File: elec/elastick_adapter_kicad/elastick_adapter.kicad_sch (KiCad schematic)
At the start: 12 parts, among them J2 DE9_Pins_MountingHoles

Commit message: update kicad
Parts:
- removed R12, R13, R14, R16, R17, R25, R26, R27, R4: 330, Resistor_THT:R_Axial_DIN0207_L6.3mm_D2.5mm_P7.62mm_Horizontal, symbol Device:R
- added C1: 470µF, Capacitor_THT:CP_Radial_D8.0mm_P3.50mm, symbol Device:C_Polarized
- added C2: 100nF, Capacitor_THT:C_Disc_D5.0mm_W2.5mm_P5.00mm, symbol Device:C
- added C3, C4: 22nF, Capacitor_THT:C_Disc_D5.0mm_W2.5mm_P5.00mm, symbol Device:C
- added J2: USB-C Breakout, elastick:usbc, symbol elastick:usbc
- added SW1: POWER, Button_Switch_THT:SW_Slide_SPDT_Angled_CK_OS102011MA1Q, symbol Switch:SW_SPDT
- added SW2: ROTARY_SWITCH, Rotary_Encoder:RotaryEncoder_Alps_EC11E-Switch_Vertical_H20mm, symbol Device:RotaryEncoder_Switch
- DS1: renamed from U2; value ~ -> SSD1306 I2C OLED
- J1: renamed from J2; value DE9_Pins_MountingHoles -> DE-9JOYSTICK
- U1: value ~ -> LOLIN-D32
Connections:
- net at J1.3: now also U1.9 (26)
- net at U1.13: now also J1.5, C4.2
- net at J1.7: now also U1.8 (25)
- net at U1.11 (14): now also J1.4
- net at U1.12: now also J1.9, C3.2
- net at DS1.1 (vcc): now also U1.1 (3v), C1.1, C2.1
- net at DS1.2 (gnd): now also U1.17 (gnd), U1.32 (gnd), C1.2, C2.2, C3.1, C4.1, SW1.1 (A), SW2.C, SW2.S1
- net at DS1.3 (scl): now also U1.22 (21)
- net at DS1.4 (sda): now also U1.21 (3)
- net at U1.10 (27): now also J1.8
- net at U1.14 (enable): now also SW1.2 (B)
- net at U1.26 (17): now also J1.2
- net at U1.27 (16): now also J1.6
- net at U1.28 (4): now also J1.1
- net at U1.5 (34): now also SW2.B
- net at U1.6 (32): now also SW2.A
- net at U1.7 (33): now also SW2.S2
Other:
- moved on the sheet: DS1, J1, U1

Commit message: update kicad
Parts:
- SW1: footprint Button_Switch_THT:SW_Slide_SPDT_Angled_CK_OS102011MA1Q -> elastick:SW_90degrees_3pins
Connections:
- net at C1.2, C2.2, C3.1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: now also SW1.2 (B), SW2.A, SW2.S2; no longer SW1.1 (A), SW2.C, SW2.S1
- net at DS1.3 (scl): now also U1.19 (22); no longer U1.22 (21)
- net at DS1.4 (sda): now also U1.22 (21); no longer U1.21 (3)
- net at U1.14 (enable): now also SW1.3 (C); no longer SW1.2 (B)
- net at U1.23 (19): now also SW2.C
- net at U1.24 (18): now also SW2.B
- net at U1.25 (5): now also SW2.S1
- net at U1.5 (34): no longer SW2.B
- net at U1.6 (32): no longer SW2.A
- net at U1.7 (33): no longer SW2.S2
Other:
- moved on the sheet: SW2

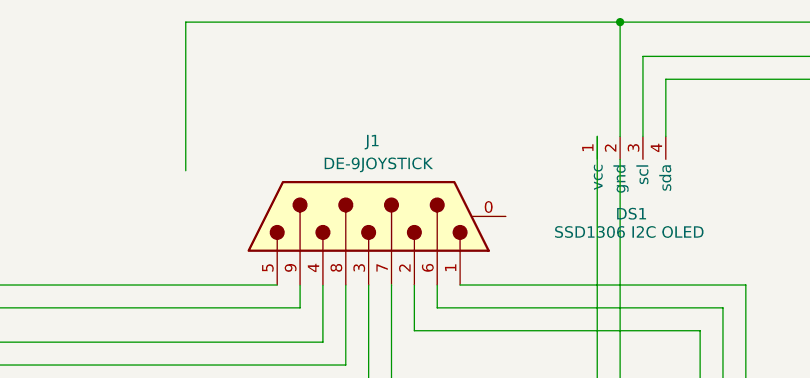
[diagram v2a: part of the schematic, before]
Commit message: update kicad with 3d for rotary button
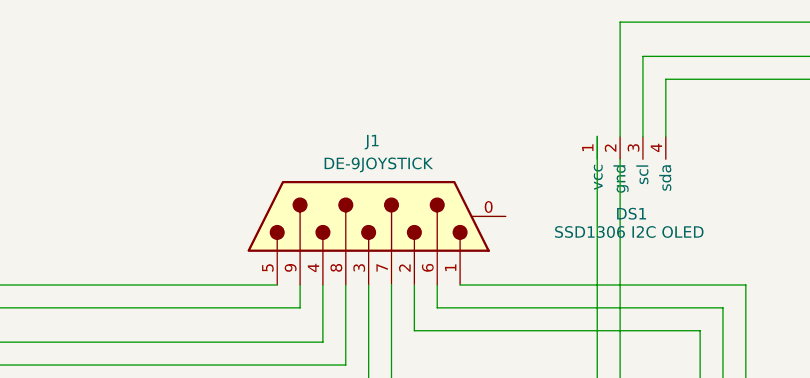
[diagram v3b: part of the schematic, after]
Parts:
- SW2: footprint Rotary_Encoder:RotaryEncoder_Alps_EC11E-Switch_Vertical_H20mm -> elastick:rotary_encoder
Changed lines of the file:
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@@
-	)
-	(junction
-		(at 179.07 16.51)
-		(diameter 0)
-		(color 0 0 0 0)
 	)
 	(junction
@@
 	(wire
 		(pts
-			(xy 130.81 16.51) (xy 130.81 33.02)
-		)
-		(stroke
-			(width 0)
-			(type default)
-		)
-	)
-	(wire
-		(pts
 			(xy 163.83 113.03) (xy 213.36 113.03)
-		)
-		(stroke
-			(width 0)
-			(type default)
-		)
-	)
-	(wire
-		(pts
-			(xy 179.07 16.51) (xy 130.81 16.51)
 		)
 		(stroke
@@
 			)
 		)
-		(property "Footprint" "Rotary_Encoder:RotaryEncoder_Alps_EC11E-Switch_Vertical_H20mm"
+		(property "Footprint" "elastick:rotary_encoder"
 			(at 224.79 85.344 0)
 			(effects

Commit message: update kicad
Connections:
- net GND_NET: now reaches C1.2, C2.2, C3.1, C4.1, DS1.2 (gnd), SW1.2 (B), SW2.A, SW2.S2, U1.17 (gnd), U1.32 (gnd)
- no-connect marks 0 -> 22
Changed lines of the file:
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@@
-	)
-	(junction
-		(at 236.22 72.39)
-		(diameter 0)
-		(color 0 0 0 0)
 	)
 	(junction
@@
 		(color 0 0 0 0)
 	)
+	(no_connect
+		(at 140.97 130.81)
+	)
+	(no_connect
+		(at 140.97 105.41)
+	)
+	(no_connect
+		(at 166.37 38.1)
+	)
+	(no_connect
+		(at 121.92 137.16)
+	)
+	(no_connect
+		(at 163.83 102.87)
+	)
+	(no_connect
+		(at 152.4 160.02)
+	)
+	(no_connect
+		(at 140.97 102.87)
+	)
+	(no_connect
+		(at 140.97 100.33)
+	)
+	(no_connect
+		(at 144.78 160.02)
+	)
+	(no_connect
+		(at 163.83 128.27)
+	)
+	(no_connect
+		(at 163.83 125.73)
+	)
+	(no_connect
+		(at 140.97 107.95)
+	)
+	(no_connect
+		(at 147.32 160.02)
+	)
+	(no_connect
+		(at 140.97 95.25)
+	)
+	(no_connect
+		(at 154.94 160.02)
+	)
+	(no_connect
+		(at 140.97 97.79)
+	)
+	(no_connect
+		(at 163.83 123.19)
+	)
+	(no_connect
+		(at 163.83 95.25)
+	)
+	(no_connect
+		(at 140.97 128.27)
+	)
+	(no_connect
+		(at 163.83 100.33)
+	)
+	(no_connect
+		(at 149.86 160.02)
+	)
+	(no_connect
+		(at 157.48 160.02)
+	)
 	(wire
 		(pts
@@
 	(wire
 		(pts
-			(xy 179.07 31.75) (xy 179.07 73.66)
-		)
-		(stroke
-			(width 0)
-			(type default)
-		)
-	)
-	(wire
-		(pts
 			(xy 179.07 92.71) (xy 228.6 92.71)
 		)
@@
 	(wire
 		(pts
+			(xy 179.07 29.21) (xy 179.07 73.66)
+		)
+		(stroke
+			(width 0)
+			(type default)
+		)
+	)
+	(wire
+		(pts
 			(xy 153.67 45.72) (xy 153.67 60.96)
 		)
@@
 	(wire
 		(pts
-			(xy 236.22 72.39) (xy 236.22 16.51)
-		)
-		(stroke
-			(width 0)
-			(type default)
-		)
-	)
-	(wire
-		(pts
 			(xy 228.6 92.71) (xy 236.22 92.71)
 		)
@@
 	(wire
 		(pts
-			(xy 236.22 16.51) (xy 179.07 16.51)
-		)
-		(stroke
-			(width 0)
-			(type default)
-		)
-	)
-	(wire
-		(pts
 			(xy 130.81 92.71) (xy 130.81 86.36)
 		)
@@
 	(wire
 		(pts
-			(xy 179.07 16.51) (xy 179.07 29.21)
-		)
-		(stroke
-			(width 0)
-			(type default)
-		)
-	)
-	(wire
-		(pts
 			(xy 163.83 105.41) (xy 207.01 105.41)
 		)
@@
 		)
 	)
+	(label "GND_NET"
+		(at 179.07 92.71 0)
+		(effects
+			(font
+				(size 1.27 1.27)
+				(color 93 61 255 1)
+			)
+			(justify left bottom)
+		)
+	)
+	(symbol
+		(lib_id "power:PWR_FLAG")
+		(at 236.22 130.81 0)
+		(unit 1)
+		(exclude_from_sim no)
+		(in_bom yes)
+		(on_board yes)
+		(dnp no)
+		(fields_autoplaced yes)
+		(property "Reference" "#FLG01"
+			(at 236.22 128.905 0)
+			(effects
+				(font
+					(size 1.27 1.27)
+				)
+				(hide yes)
+			)
+		)
+		(property "Value" "PWR_FLAG"
+			(at 236.22 125.73 0)
+			(effects
+				(font
+					(size 1.27 1.27)
+				)
+			)
+		)
+		(property "Footprint" ""
+			(at 236.22 130.81 0)
+			(effects
+				(font
+					(size 1.27 1.27)
+				)
+				(hide yes)
+			)
+		)
+		(property "Datasheet" "~"
+			(at 236.22 130.81 0)
+			(effects
+				(font
+					(size 1.27 1.27)
+				)
+				(hide yes)
+			)
+		)
+		(property "Description" "Special symbol for telling ERC where power comes from"
+			(at 236.22 130.81 0)
+			(effects
+				(font
+					(size 1.27 1.27)
+				)
+				(hide yes)
+			)
+		)
+		(pin "1"
+		)
+		(instances
+			(project ""
+				(path "/8b1d5b76-5ba4-41f6-b01f-dd3399f06215"
+					(reference "#FLG01")
+					(unit 1)
+				)
+			)
+		)
+	)

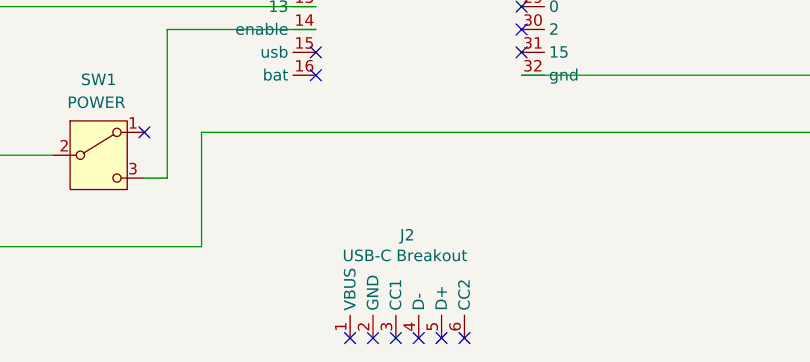
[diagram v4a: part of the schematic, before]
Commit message: make pcb more compact (+ removed usb-c adapter)
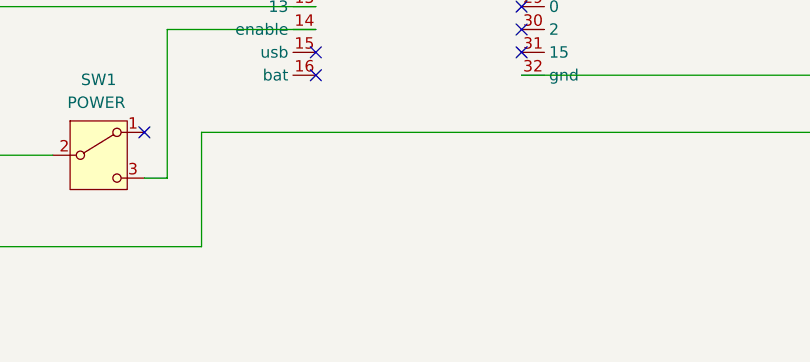
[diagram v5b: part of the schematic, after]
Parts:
- removed J2: USB-C Breakout, elastick:usbc, symbol elastick:usbc
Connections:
- no-connect marks 22 -> 16
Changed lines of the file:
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@@
-	)
-	(no_connect
-		(at 152.4 160.02)
 	)
 	(no_connect
@@
 	)
 	(no_connect
-		(at 144.78 160.02)
-	)
-	(no_connect
 		(at 163.83 128.27)
 	)
@@
 	)
 	(no_connect
-		(at 147.32 160.02)
-	)
-	(no_connect
 		(at 140.97 95.25)
-	)
-	(no_connect
-		(at 154.94 160.02)
 	)
 	(no_connect
@@
 	(no_connect
 		(at 163.83 100.33)
-	)
-	(no_connect
-		(at 149.86 160.02)
-	)
-	(no_connect
-		(at 157.48 160.02)
 	)
 	(wire
@@
 					(unit 1)
 				)
-			)
-		)
-	)
-	(symbol
-		(lib_id "elastick:usbc")
-		(at 144.78 160.02 0)
-		(unit 1)
-		(exclude_from_sim no)
-		(in_bom yes)
-		(on_board yes)
-		(dnp no)
-		(property "Reference" "J2"
-			(at 151.13 148.59 0)
-			(effects
-				(font
-					(size 1.27 1.27)
-				)
-			)
-		)
-		(property "Value" "USB-C Breakout"
-			(at 150.876 150.876 0)
-			(effects
-				(font
-					(size 1.27 1.27)
-				)
-			)
-		)
-		(property "Footprint" "elastick:usbc"
-			(at 144.78 160.02 0)
-			(effects
-				(font
-					(size 1.27 1.27)
-				)
-				(hide yes)
-			)
-		)
-		(property "Datasheet" ""
-			(at 144.78 160.02 0)
-			(effects
-				(font
-					(size 1.27 1.27)
-				)
-				(hide yes)
-			)
-		)
-		(property "Description" ""
-			(at 144.78 160.02 0)
-			(effects
-				(font
-					(size 1.27 1.27)
-				)
-				(hide yes)
-			)
-		)
-		(pin "5"
-		)
-		(pin "3"
-		)
-		(pin "4"
-		)
-		(pin "1"
-		)
-		(pin "2"
-		)
-		(pin "6"
-		)
-		(instances
-			(project ""
-				(path "/8b1d5b76-5ba4-41f6-b01f-dd3399f06215"
-					(reference "J2")
-					(unit 1)
-				)
